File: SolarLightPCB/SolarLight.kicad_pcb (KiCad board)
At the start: 2 copper layers, 92 x 36.3 mm, 15 parts, among them J1 I2C, J2 Conn_01x06_Male, SW1 SW_Push, SW2 ON_OFF, U1 TP4056, U2 WeMos_D1_mini

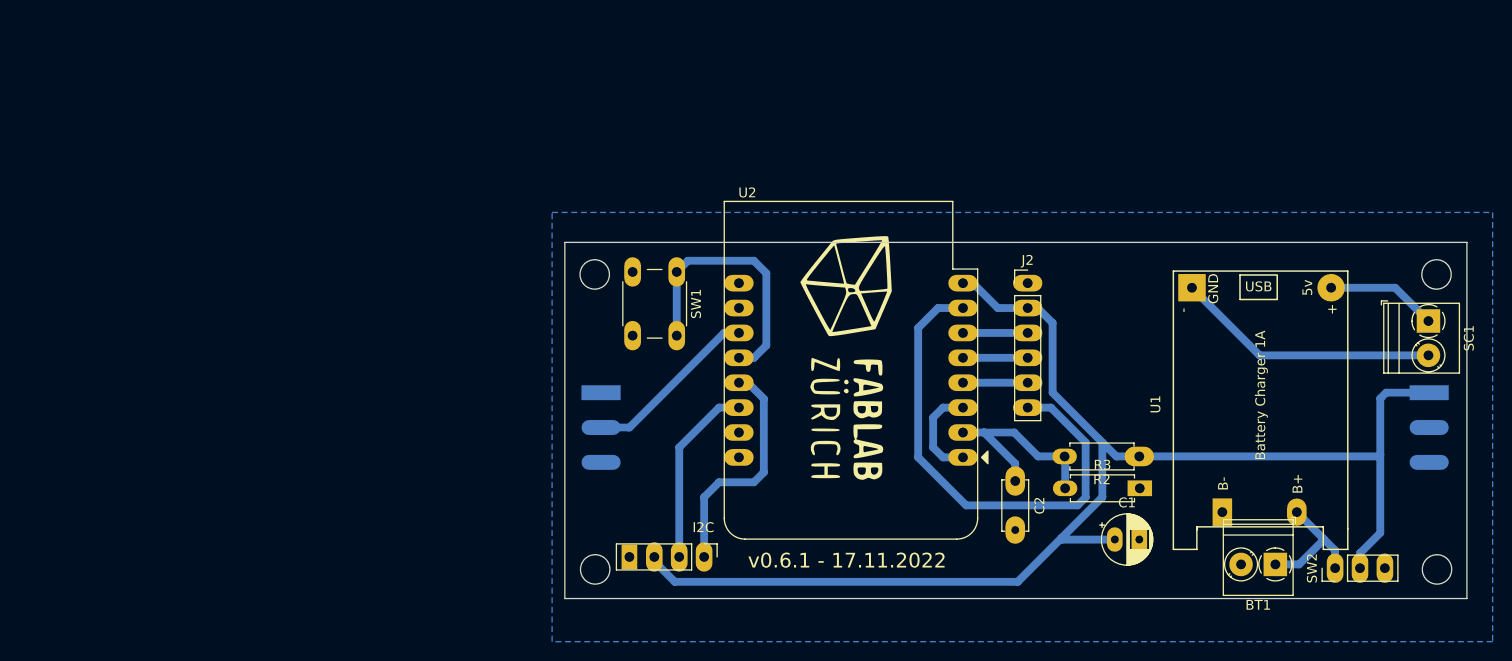
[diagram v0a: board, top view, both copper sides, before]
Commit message: Add 1mm tracks
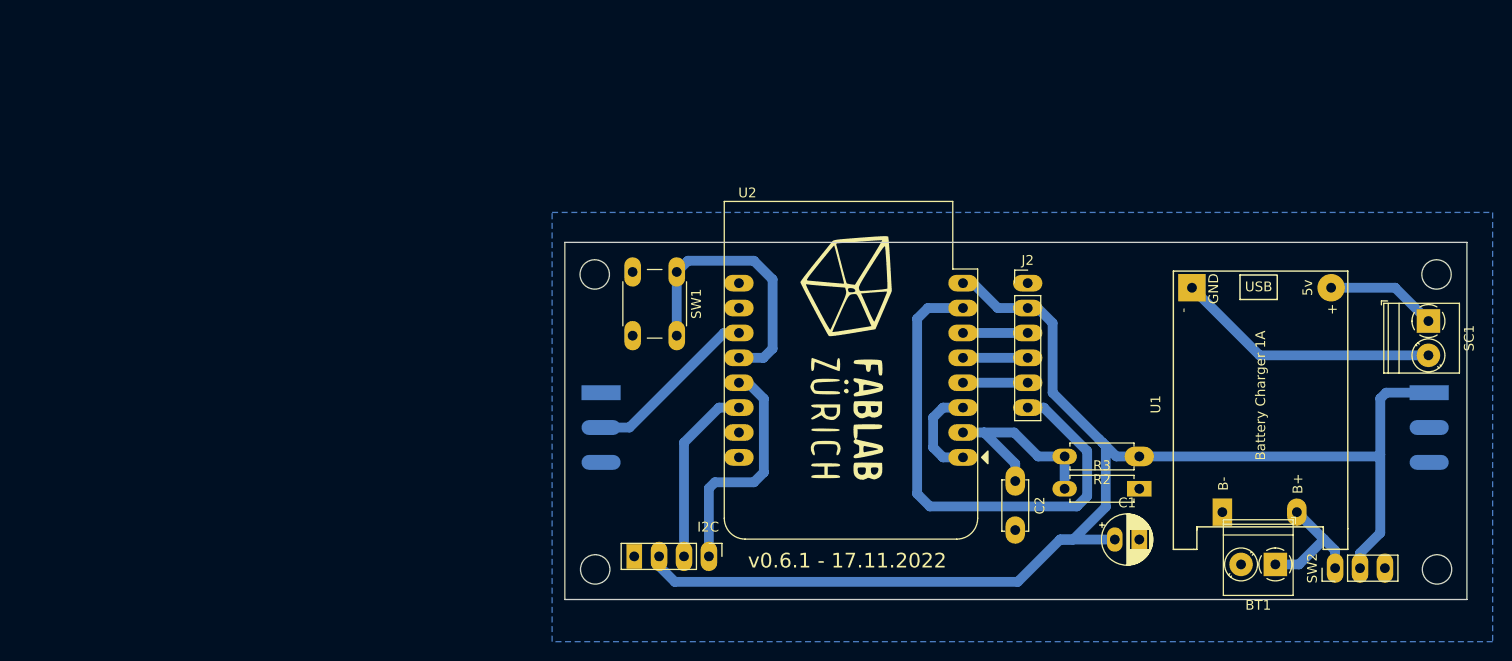
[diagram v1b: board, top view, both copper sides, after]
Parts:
- moved J1 0.49 mm to (96.5, 92.4)
- moved R3 0.07 mm to (132.8, 85.5)
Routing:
- net CS: track 51.1 -> 53.8 mm
- net SWITCH: track 27.3 -> 28.4 mm
- net BATTERY: track 139.3 -> 140.3 mm
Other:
- board size 92 x 36.3 mm -> 92 x 36.4 mm

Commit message: Move the I2C and ON-OFF jumper closer to the edge
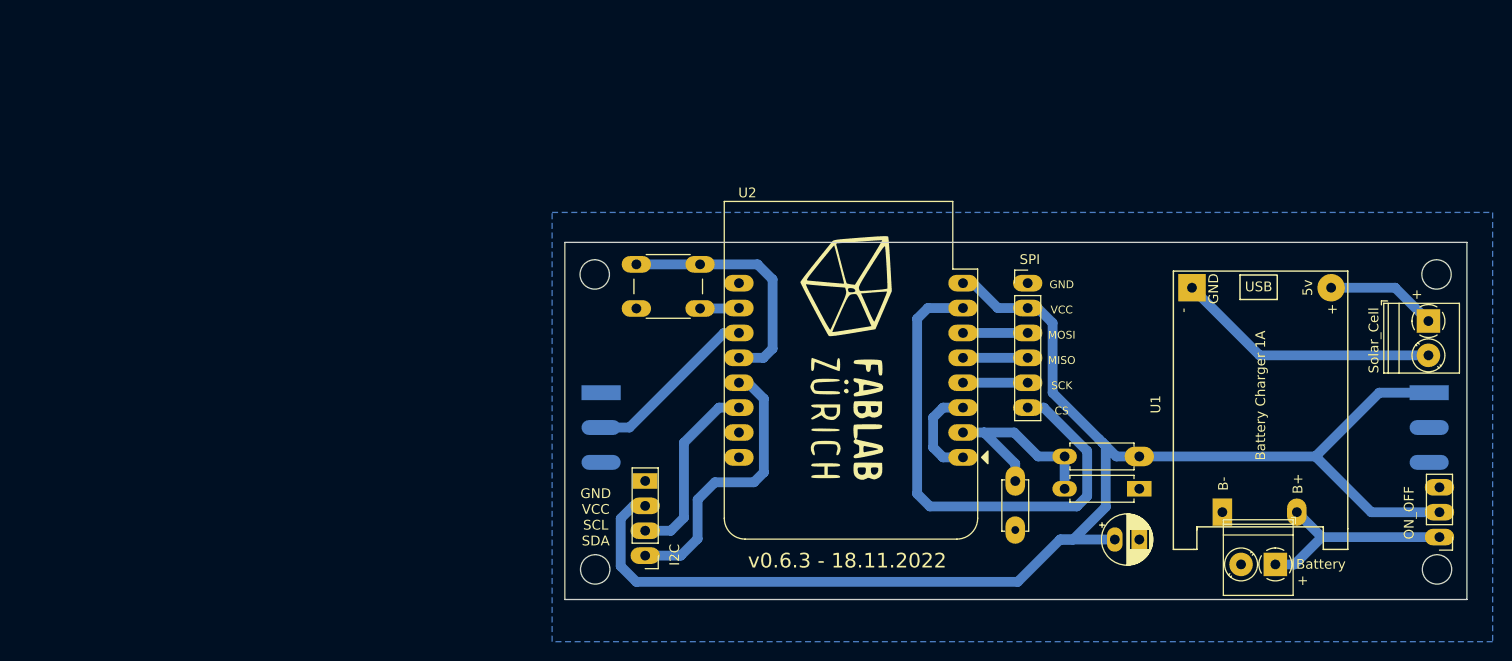
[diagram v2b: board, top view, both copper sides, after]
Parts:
- BT1: value Battery_Cell -> Battery
- J2: value Conn_01x06_Male -> SPI
- moved SW2 11.1 mm to (171.1, 90.4), turned to 180 degrees
- moved J1 6.50 mm to (90.0, 92.3), turned to 180 degrees
- moved SW1 4.19 mm to (89.1, 62.6), turned to 0 degrees
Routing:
- net BATTERY: track 140.3 -> 150.3 mm
- net Net-(BT1-Pad1): track 13.4 -> 21.5 mm
- net SDA: track 24.0 -> 28.7 mm
- net GND: track 0.00 -> 3.99 mm
- net SWITCH: track 28.4 -> 25.4 mm
- net SCL: track 18.7 -> 19.3 mm
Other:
- board text added: "+"
- board text added: "GND VCC MOSI MISO SCK CS"
- board text added: "GND VCC SCL SDA"
- board text added: "v0.6.3 - 18.11.2022"
- board text removed: "v0.6.1 - 17.11.2022"

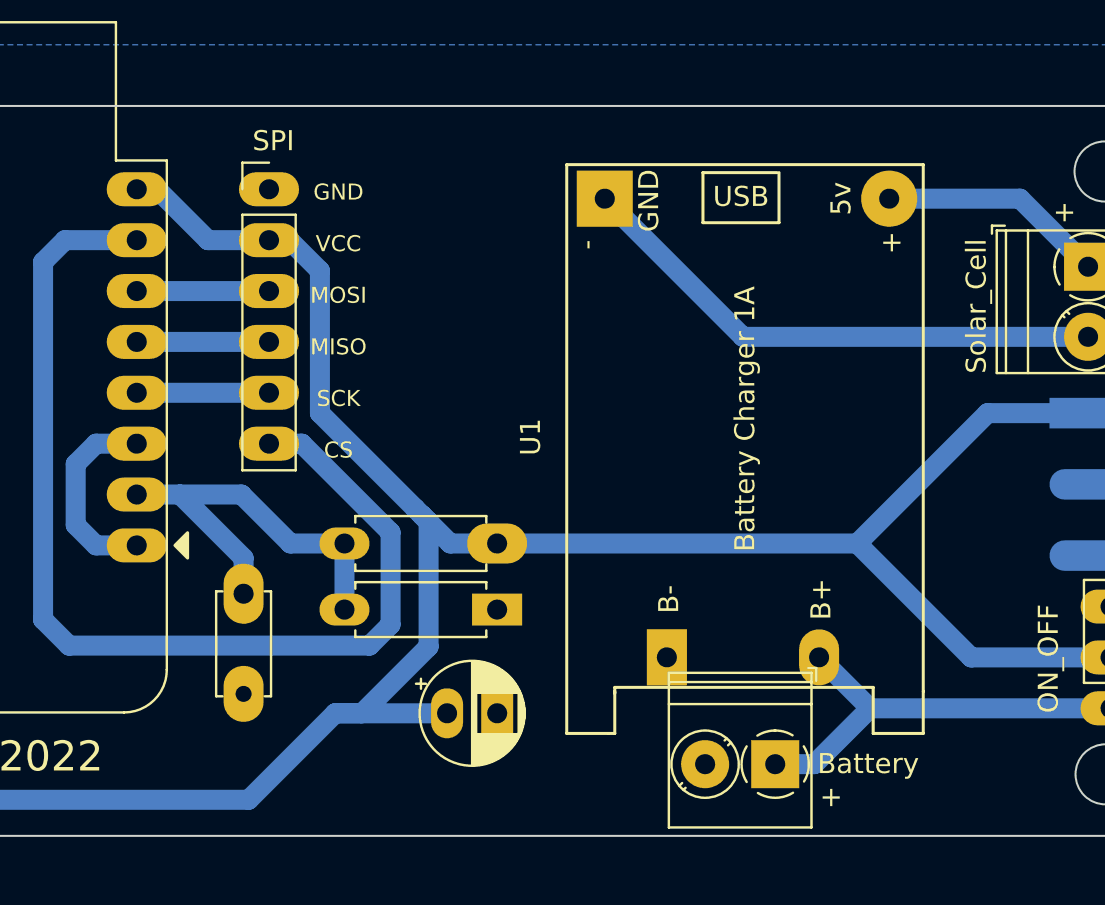
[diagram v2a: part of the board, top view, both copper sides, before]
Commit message: Add the missing capacitor to the schema
Fixing the warning because the pad of the charger module was removed
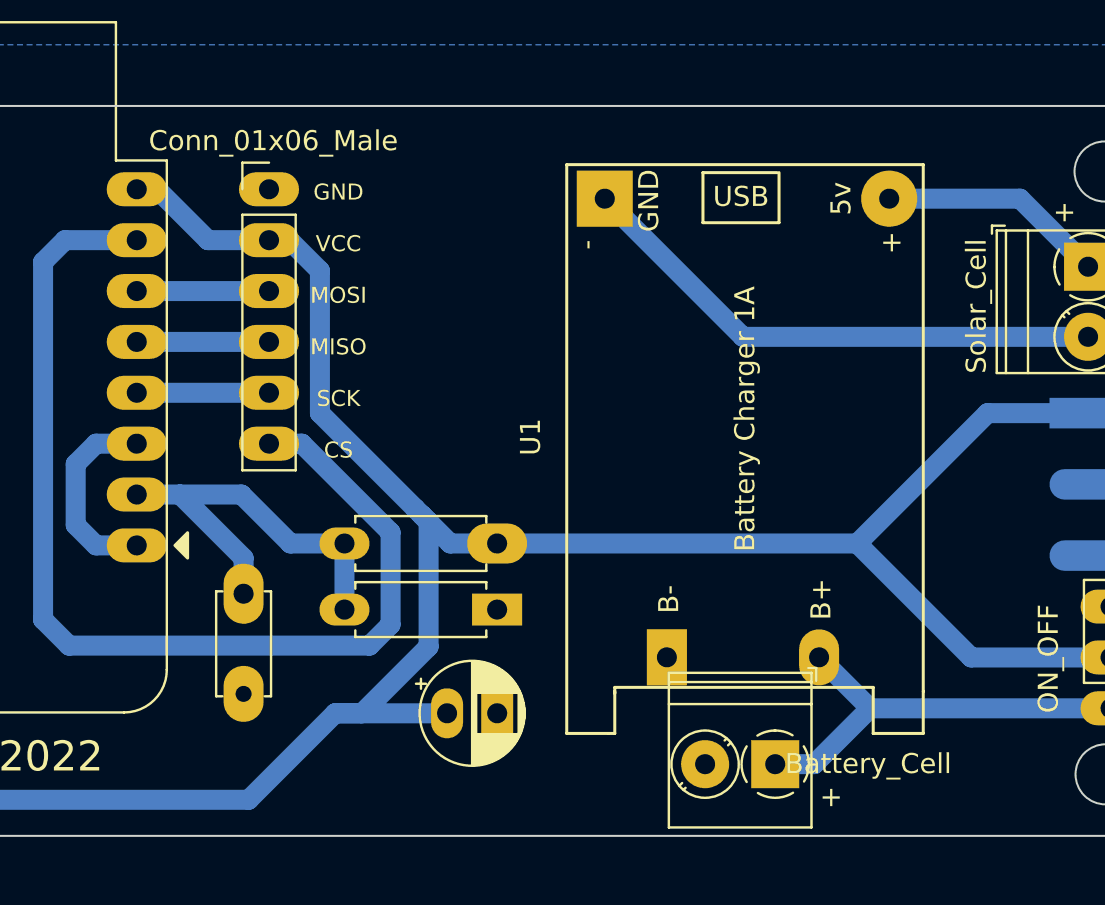
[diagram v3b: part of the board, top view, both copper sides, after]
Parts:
- BT1: value Battery -> Battery_Cell
- C2: value C -> 100nF
- J2: value SPI -> Conn_01x06_Male
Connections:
- C2 pad 1: A0 -> unconnected-(C2-Pad1)
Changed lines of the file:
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@@
   (net 19 "Net-(BT1-Pad1)")
   (net 20 "SWITCH")
+  (net 21 "unconnected-(C2-Pad1)")
   (footprint "Connector_PinHeader_2.54mm:PinHeader_1x04_P2.54mm_Vertical" (layer "F.Cu")
     (at 90 92.32 180)
@@
       (effects (font (size 1 1) (thickness 0.15)))
     )
-    (fp_text value "SPI" (at 0.218 -2.416) (layer "F.SilkS")
+    (fp_text value "Conn_01x06_Male" (at 0.218 -2.416) (layer "F.SilkS")
       (effects (font (size 1 1) (thickness 0.15)))
     )
@@
       (effects (font (size 1 1) (thickness 0.15)))
     )
-    (fp_text value "Battery" (at -4.645 0.018) (layer "F.SilkS")
+    (fp_text value "Battery_Cell" (at -4.645 0.018) (layer "F.SilkS")
       (effects (font (size 1 1) (thickness 0.15)))
     )
@@
       (effects (font (size 1 1) (thickness 0.15)))
     )
-    (fp_text value "C" (at 2.5 2.5 90) (layer "F.Fab")
+    (fp_text value "100nF" (at 2.5 2.5 90) (layer "F.Fab")
       (effects (font (size 1 1) (thickness 0.15)))
     )
@@
     (fp_line (start 5 1.25) (end 5 -1.25) (layer "F.Fab") (width 0.1))
     (pad "1" thru_hole oval (at 0 0 270) (size 3 2) (drill 1) (layers *.Cu *.Mask)
-      (net 16 "A0") (pintype "passive"))
+      (net 21 "unconnected-(C2-Pad1)") (pintype "passive"))
     (pad "2" thru_hole oval (at 5 0 270) (size 2.8 2) (drill 0.8) (layers *.Cu *.Mask)
       (net 2 "GND") (pintype "passive"))

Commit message: Update silkscreen
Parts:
- J2: value Conn_01x06_Male -> SPI
- SW1: value SW_Push -> Switch
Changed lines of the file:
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@@
       (effects (font (size 1 1) (thickness 0.15)))
     )
-    (fp_text value "Conn_01x06_Male" (at 0.218 -2.416) (layer "F.SilkS")
+    (fp_text value "SPI" (at 0.218 -2.416) (layer "F.SilkS")
       (effects (font (size 1 1) (thickness 0.15)))
     )
@@
       (effects (font (size 1 1) (thickness 0.15)))
     )
-    (fp_text value "SW_Push" (at 3.75 6.7) (layer "F.Fab")
+    (fp_text value "Switch" (at 3.75 6.7) (layer "F.Fab")
       (effects (font (size 1 1) (thickness 0.15)))
     )

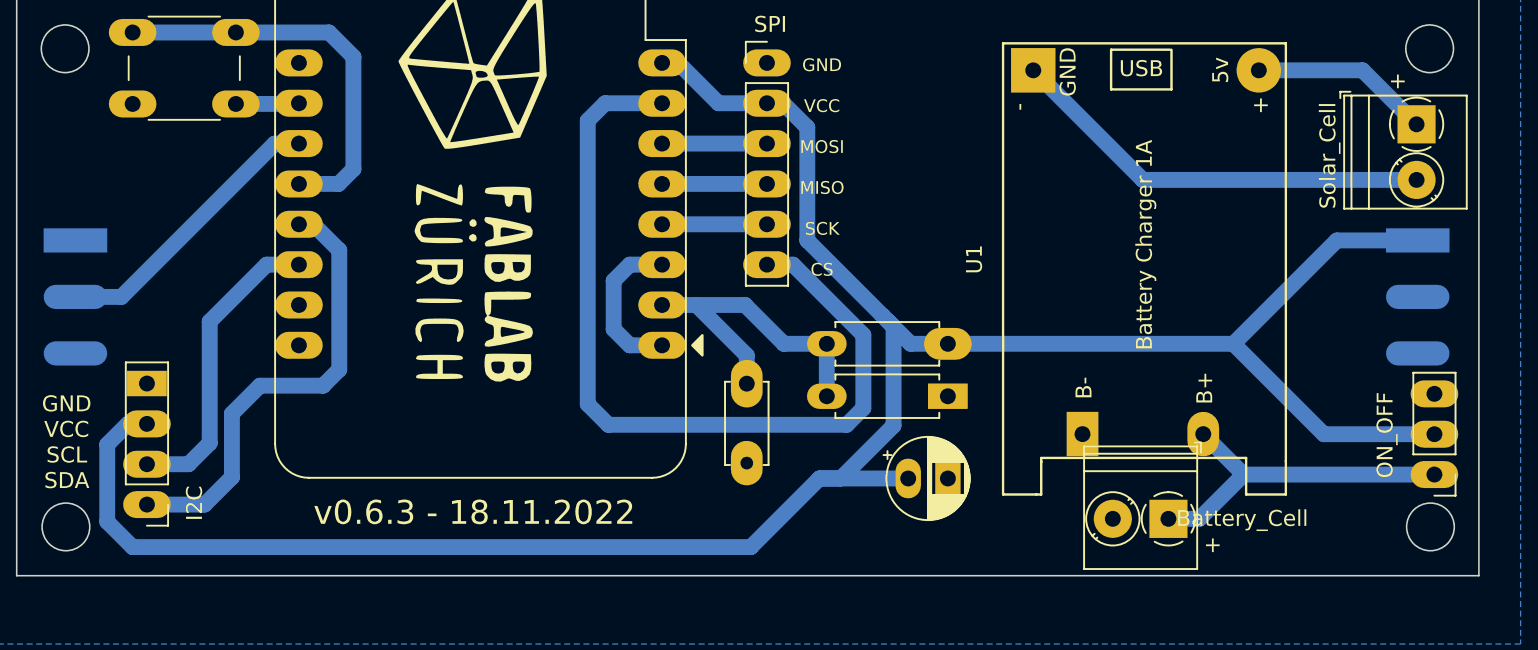
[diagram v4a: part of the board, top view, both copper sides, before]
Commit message: Added diode for reducing the voltage of the battery to ~3.3V
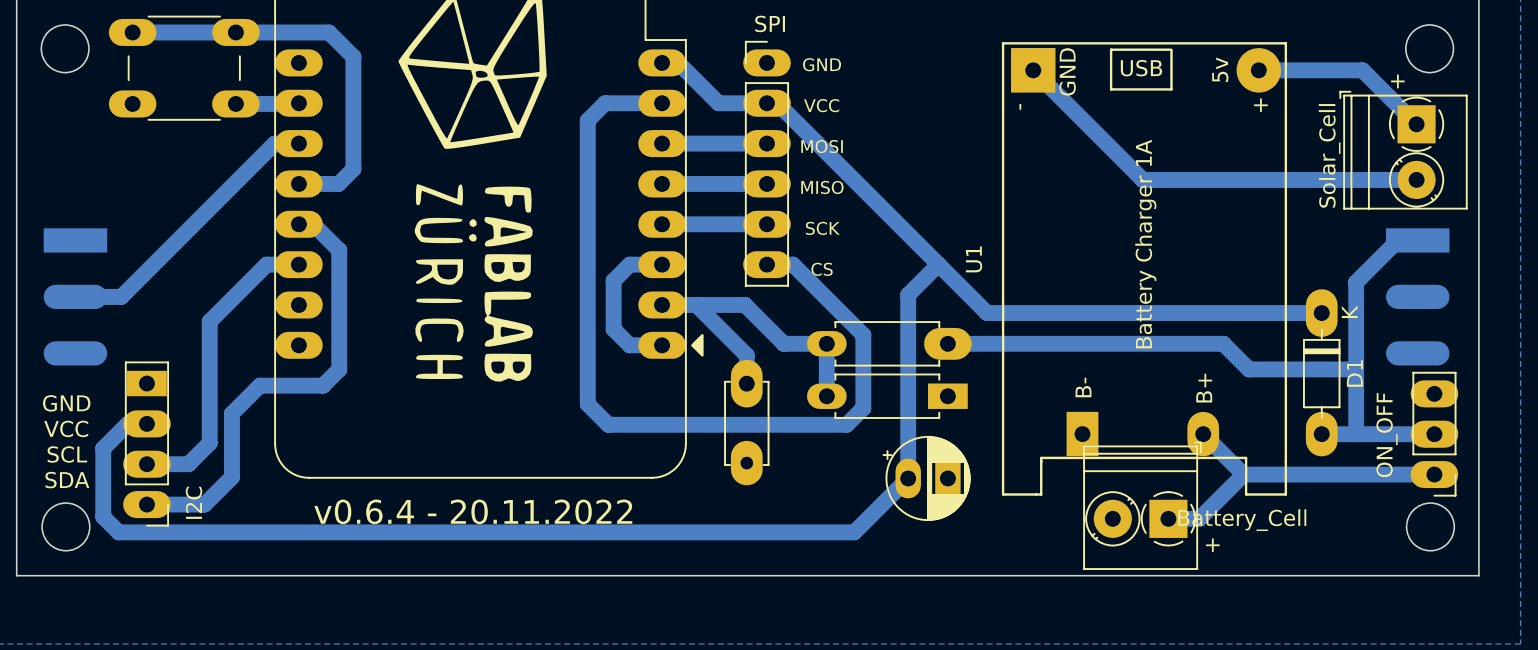
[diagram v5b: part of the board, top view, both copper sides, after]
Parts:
- added D1: 1N4148, Diode_THT:D_DO-35_SOD27_P7.62mm_Horizontal, F.Cu at (164.0, 80.3)
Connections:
- C1 pad 1: BATTERY -> +3V3
- C2 pad 1: unconnected-(C2-Pad1) -> A0
- J1 pad 3: BATTERY -> +3V3
- J2 pad 2: BATTERY -> +3V3
- U2 pad 8: BATTERY -> +3V3
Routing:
- net +3V3: track 0.00 -> 122.5 mm
- net BATTERY: track 150.3 -> 48.5 mm
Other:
- board text added: "v0.6.4 - 20.11.2022"
- board text removed: "v0.6.3 - 18.11.2022"

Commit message: Update schematics and bump to version 0.7
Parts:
- added R1: 100k, Resistor_THT:R_Axial_DIN0207_L6.3mm_D2.5mm_P7.62mm_Horizontal, F.Cu at (146.8, 94.0)
- moved C1 24.2 mm to (134.6, 66.7), turned to 90 degrees
- moved J1 1.48 mm to (90.9, 93.5)
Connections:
- BT1 pad 1: Net-(BT1-Pad1) -> BATTERY
- BT1 pad 2: GND -> Net-(BT1-Pad2)
- D1 pad 2: BATTERY -> /VNEO
- LIN1 pad 1: BATTERY -> /VNEO
- SW2 pad 1: Net-(BT1-Pad1) -> Net-(SW2-Pad1)
- SW2 pad 2: BATTERY -> /VNEO
- U1 pad 5: Net-(BT1-Pad1) -> BATTERY
- U1 pad 6: GND -> Net-(BT1-Pad2)
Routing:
- net BATTERY: track 48.5 -> 24.9 mm
- net /VNEO: track 0.00 -> 22.1 mm
- net Net-(BT1-Pad1): track 21.5 -> 0.00 mm
- net Net-(SW2-Pad1): track 0.00 -> 12.1 mm
- net Net-(BT1-Pad2): track 0.00 -> 9.66 mm
- net +3V3: track 122.5 -> 128.7 mm
- net CS: track 53.8 -> 50.0 mm
- net A0: track 21.0 -> 18.2 mm
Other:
- board text added: "v0.7 - 19.12.2022"
- board text removed: "v0.6.4 - 20.11.2022"
